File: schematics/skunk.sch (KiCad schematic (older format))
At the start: 37 parts

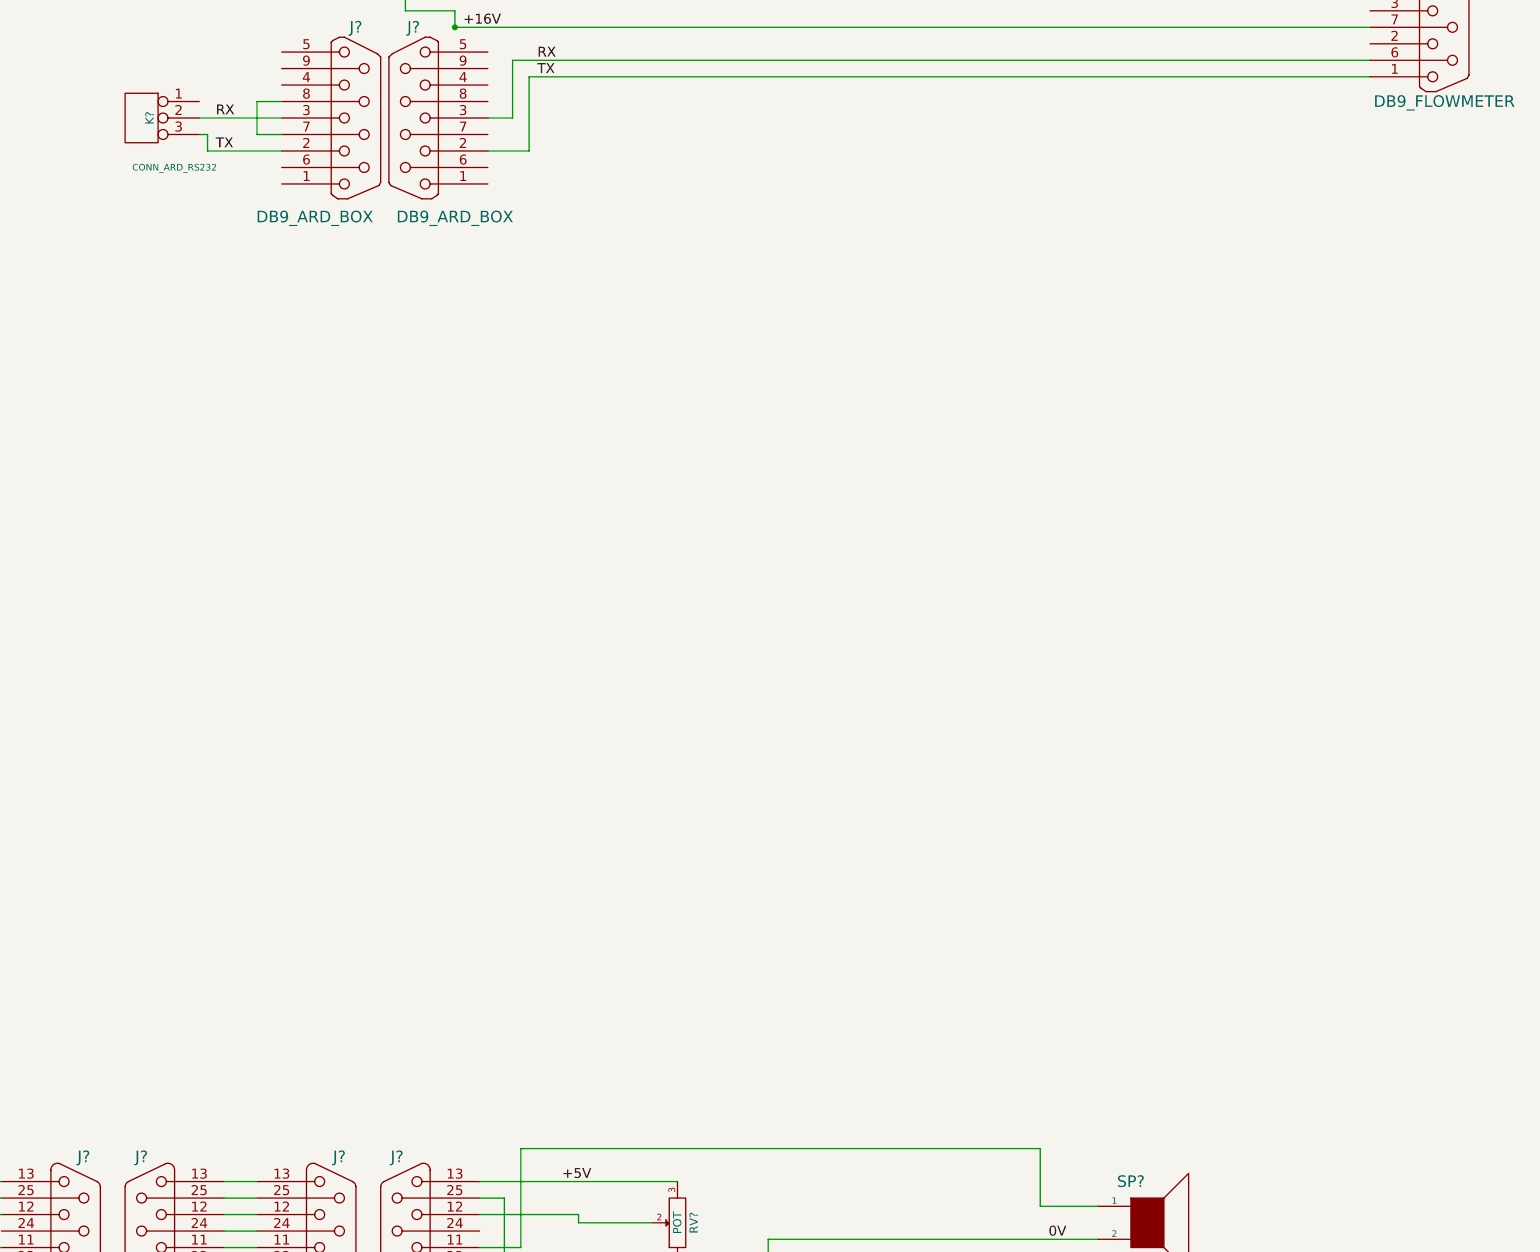
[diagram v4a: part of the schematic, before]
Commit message: Added schem sheet annotation and labels
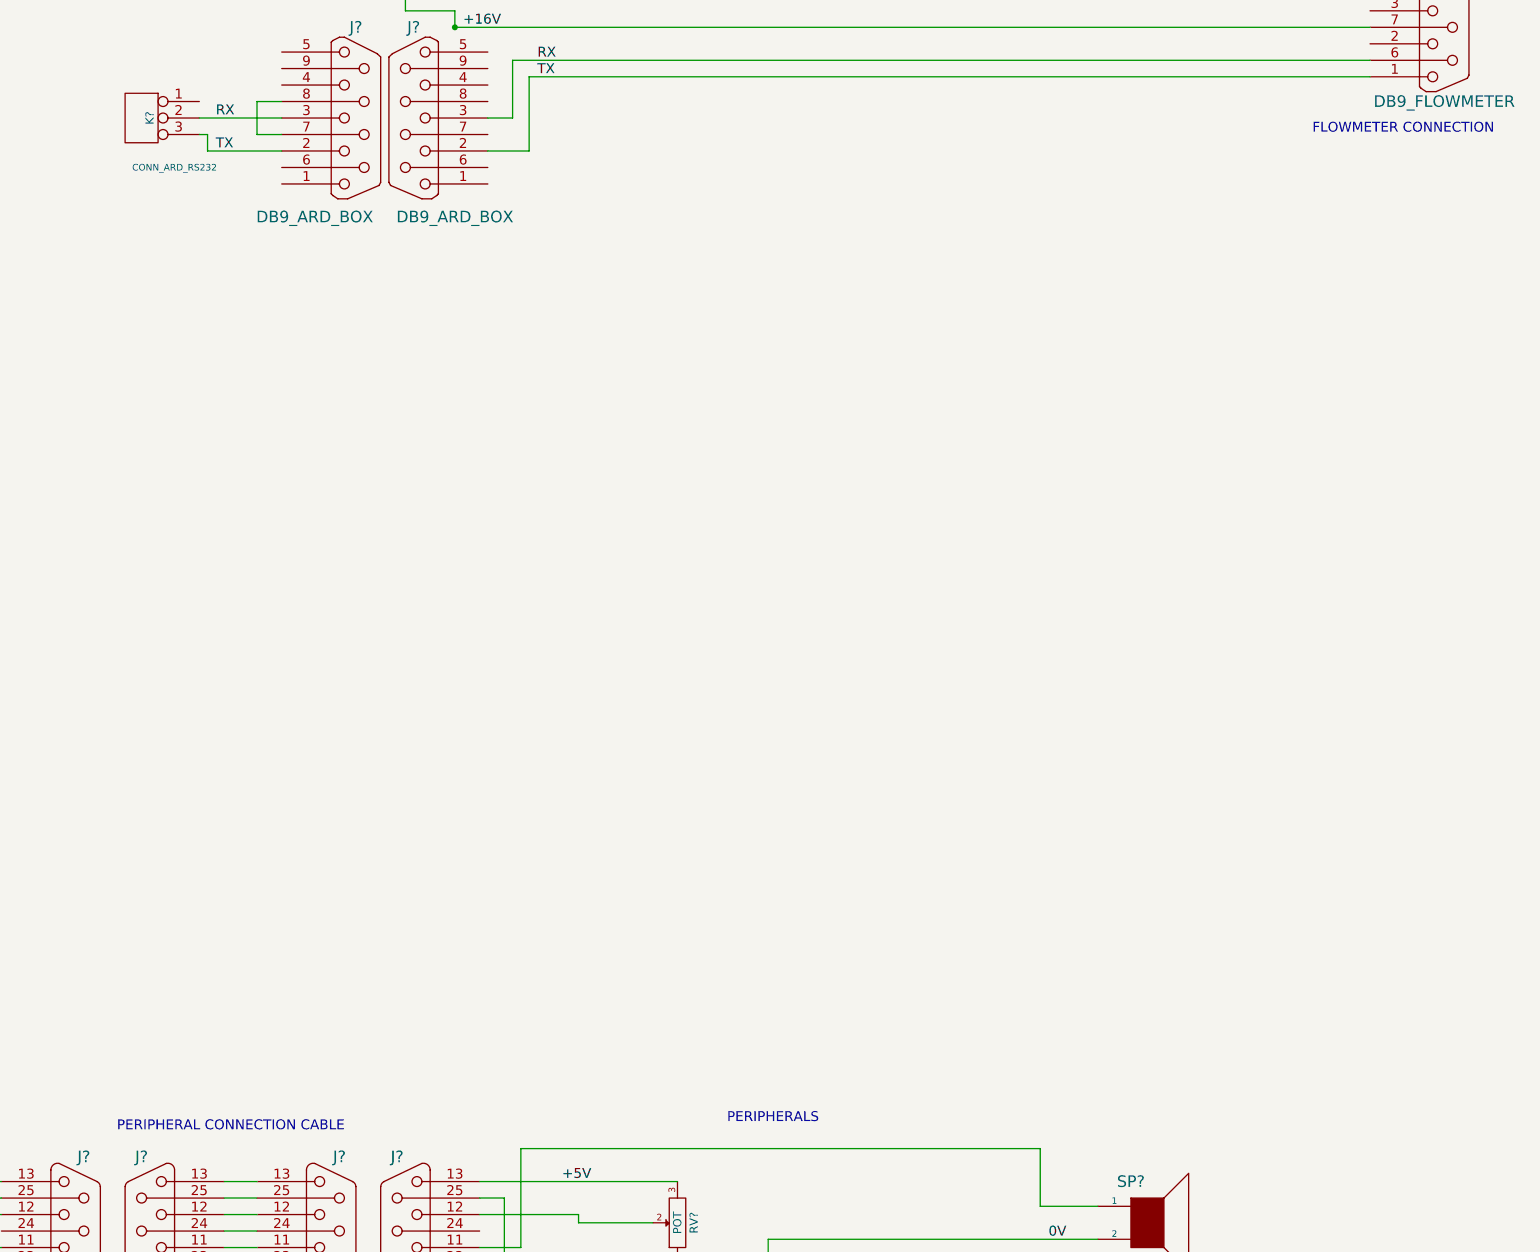
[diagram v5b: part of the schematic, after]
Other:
- note added: "FLOWMETER CONNECTION"
- note added: "PERIPHERAL CONNECTION CABLE"
- note added: "PERIPHERALS"
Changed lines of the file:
@@
-EESchema Schematic File Version 2  date Fri 05 Oct 2012 15:36:33 BST
+EESchema Schematic File Version 2  date Fri 05 Oct 2012 15:40:29 BST
 LIBS:power
 LIBS:device
@@
 encoding utf-8
 Sheet 1 1
-Title ""
+Title "SKUNK WIRING HARNESS AND SCHEMATIC"
 Date "5 oct 2012"
 Rev ""
-Comp ""
+Comp "CAMBRIDGE UNIVERSITY SPACE FLIGHT - dwt27"
 Comment1 ""
 Comment2 ""
@@
 IDIOT\nDIODE
 Connection ~ 5300 750
+Text Notes 14700 1900 0    60   ~ 0
+FLOWMETER CONNECTION
+Text Notes 7450 7950 0    60   ~ 0
+PERIPHERAL CONNECTION CABLE
+Text Notes 11150 7900 0    60   ~ 0
+PERIPHERALS
 $EndSCHEMATC
